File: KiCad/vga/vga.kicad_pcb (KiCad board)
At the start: 4 copper layers, 160 x 111.8 mm, 90 parts, among them J1 VGA connector, J2 JTAG, U1 EPM240T100, U10 74HC245, U11 74HC245, U12 74AC573, U13 74AC573, U14 EPM7064S, U15 74AC573, U16 74AC573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

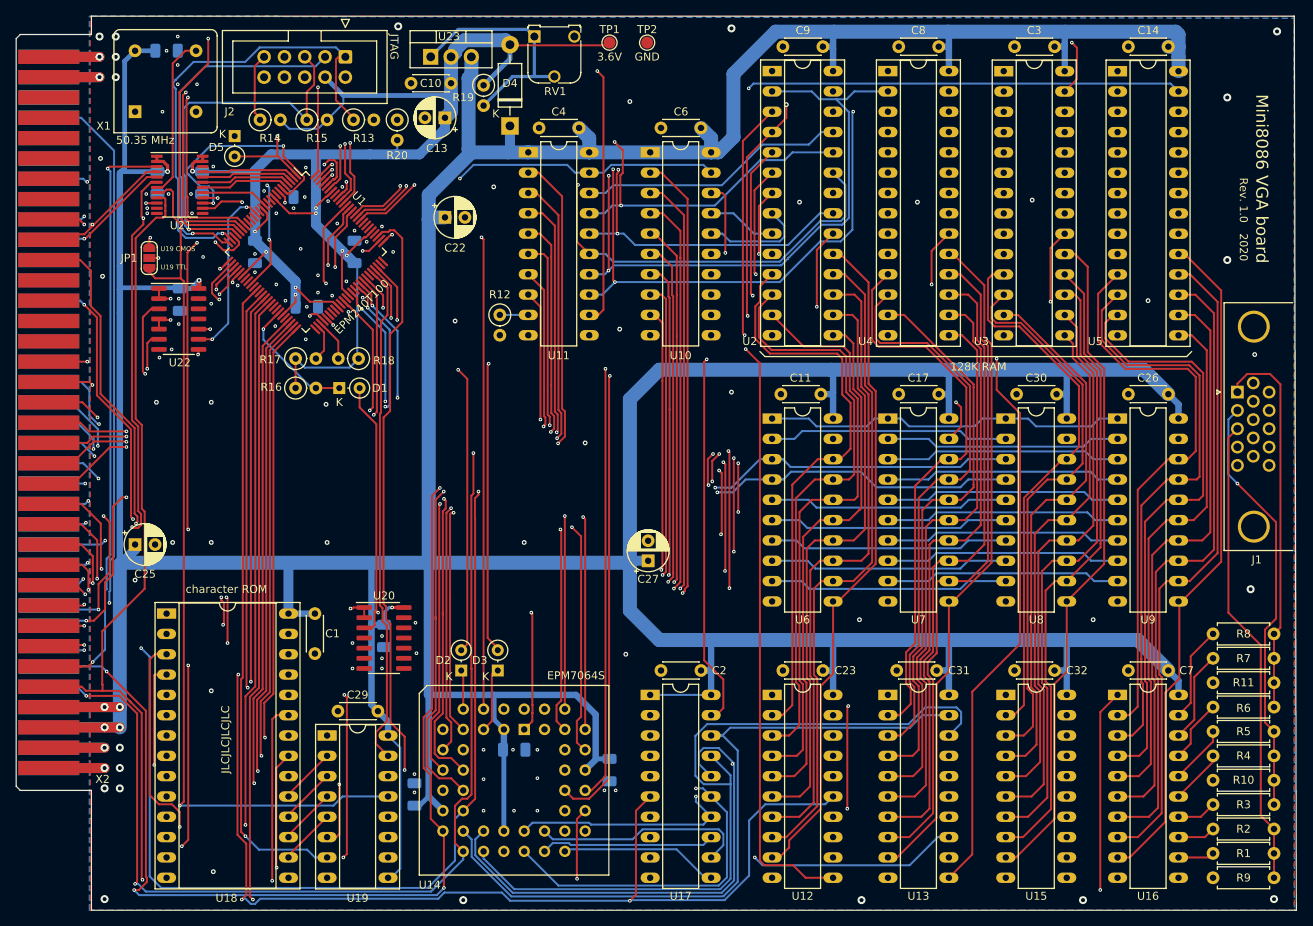
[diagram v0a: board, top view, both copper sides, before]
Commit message: Minor changes at I/O board, LED board and VGA
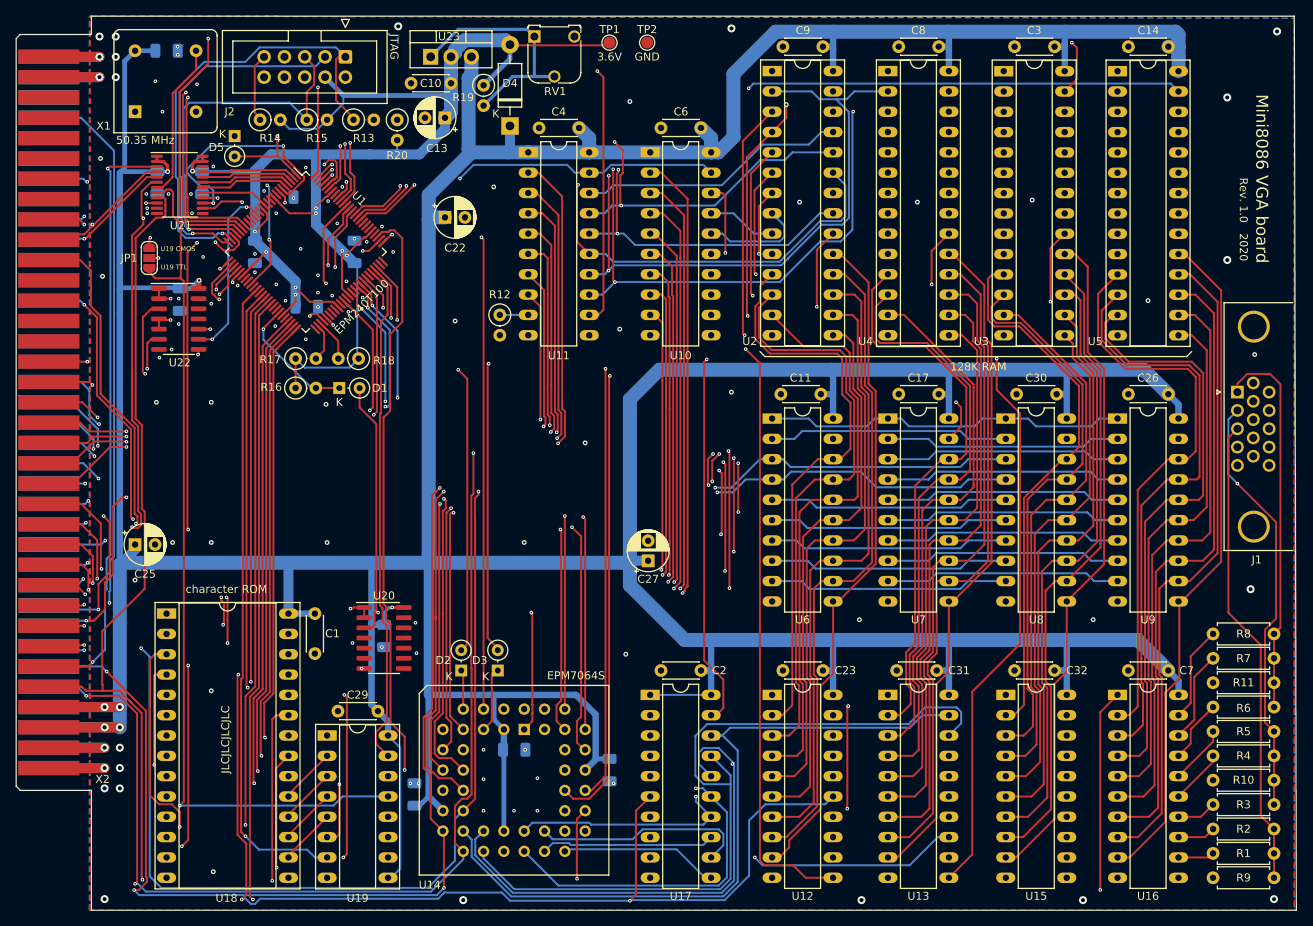
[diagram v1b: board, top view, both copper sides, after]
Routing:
- net VCC: track 795.2 -> 793.3 mm
- net /CPLD/TCK: track 59.7 -> 58.6 mm
- net /CPLD/CPLD_CLK: track 20.3 -> 19.5 mm
- net ~WE_R1: track 121.7 -> 122.3 mm
- net GND: vias 114 -> 108
